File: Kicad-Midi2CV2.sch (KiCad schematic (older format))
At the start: 101 parts, among them IC101 MCP4725module, IC102 MCP4725module, J101 Doepfer connector, J102 Vin 7-12v, J103 MIDI OUT, J104 Power Conn, J105 CV7 in, J106 Gate1, J107 MIDI IN, J108 CV6 in, J109 Gate2, J110 CV3 in, J111 Gate3, J112 CV1, J113 Gate4, J114 CV2, J115 ControlConn, J116 ControlConn, J117 I2C_Conn, J118 I2C_Conn, Q101 MMBT2222A, Q102 MMBT2222A, SW101 KY40_Rotary_Encoder_Module, U101 TL072, U102 TL072, U103 EL814

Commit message: Kicad faliure - unknown state
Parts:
- added D?: LEDset1, LED_THT:LED_D3.0mm_Horizontal_O6.35mm_Z6.0mm, symbol Device:LED
- added R?: 680R, Resistor_SMD:R_0805_2012Metric_Pad1.15x1.40mm_HandSolder, symbol Device:R
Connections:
- wire segments 420 -> 424
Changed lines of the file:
@@
 Text Notes 650  3200 0    79   ~ 16
 MIDI IN
-Text Notes 2875 6125 0    79   ~ 16
+Text Notes 2900 6675 0    79   ~ 16
 LED Signals
 Text Notes 800  6900 0    79   ~ 16
@@
 	750  6300 750  6600
 Wire Wire Line
-	750  5975 750  6300
+	750  5975 750  6100
 Wire Wire Line
 	750  6600 750  7400
@@
 	6550 1350 6550 1175
 Connection ~ 6550 1350
+Text GLabel 3250 6100 2    50   Input ~ 0
+LED_LFO
+$Comp
+L Device:LED D?
+U 1 1 5C593F89
+P 2525 6100
+F 0 "D?" H 2516 6316 50  0000 C CNN
+F 1 "LEDset1" H 2516 6225 50  0000 C CNN
+F 2 "LED_THT:LED_D3.0mm_Horizontal_O6.35mm_Z6.0mm" H 2525 6100 50  0001 C CNN
+F 3 "~" H 2525 6100 50  0001 C CNN
+	1    2525 6100
+	1    0    0    -1
+$EndComp
+$Comp
+L Device:R R?
+U 1 1 5C593F8F
+P 2975 6100
+F 0 "R?" V 2768 6100 50  0000 C CNN
+F 1 "680R" V 2859 6100 50  0000 C CNN
+F 2 "Resistor_SMD:R_0805_2012Metric_Pad1.15x1.40mm_HandSolder" V 2905 6100 50  0001 C CNN
+F 3 "~" H 2975 6100 50  0001 C CNN
+	1    2975 6100
+	0    1    1    0
+$EndComp
+Wire Wire Line
+	2825 6100 2675 6100
+Wire Wire Line
+	3125 6100 3250 6100
+Wire Wire Line
+	2375 6100 750  6100
+Connection ~ 750  6100
+Wire Wire Line
+	750  6100 750  6300
 $EndSCHEMATC

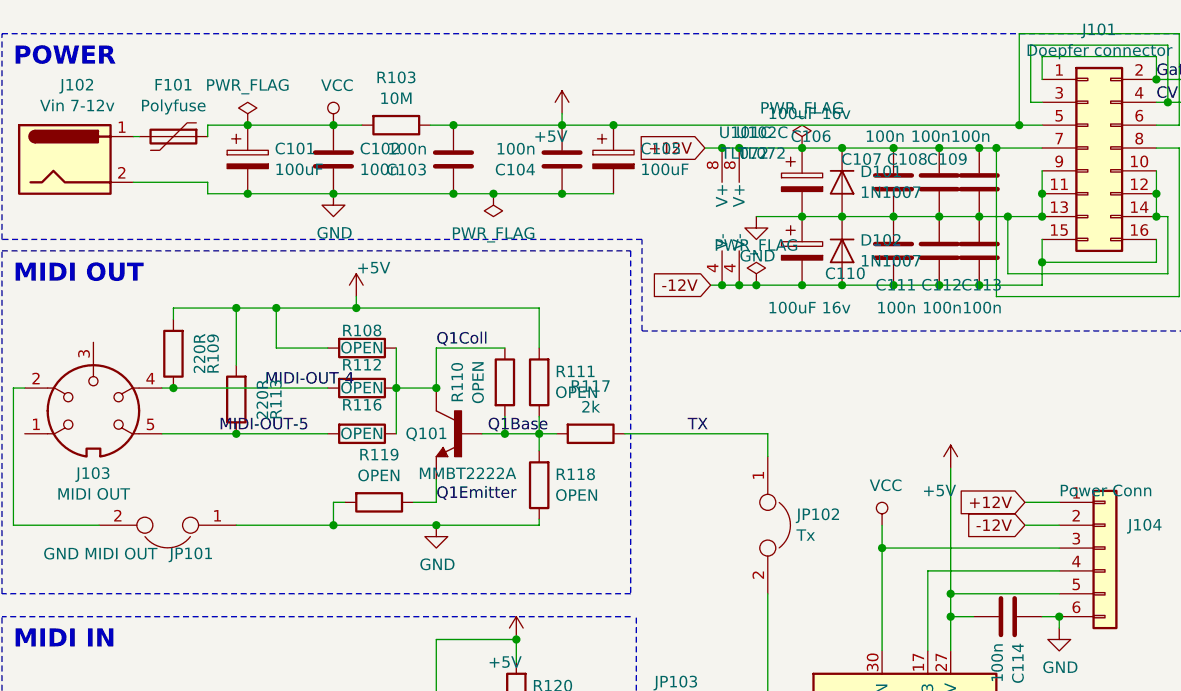
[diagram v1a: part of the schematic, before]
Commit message: Footprints and MIDI out
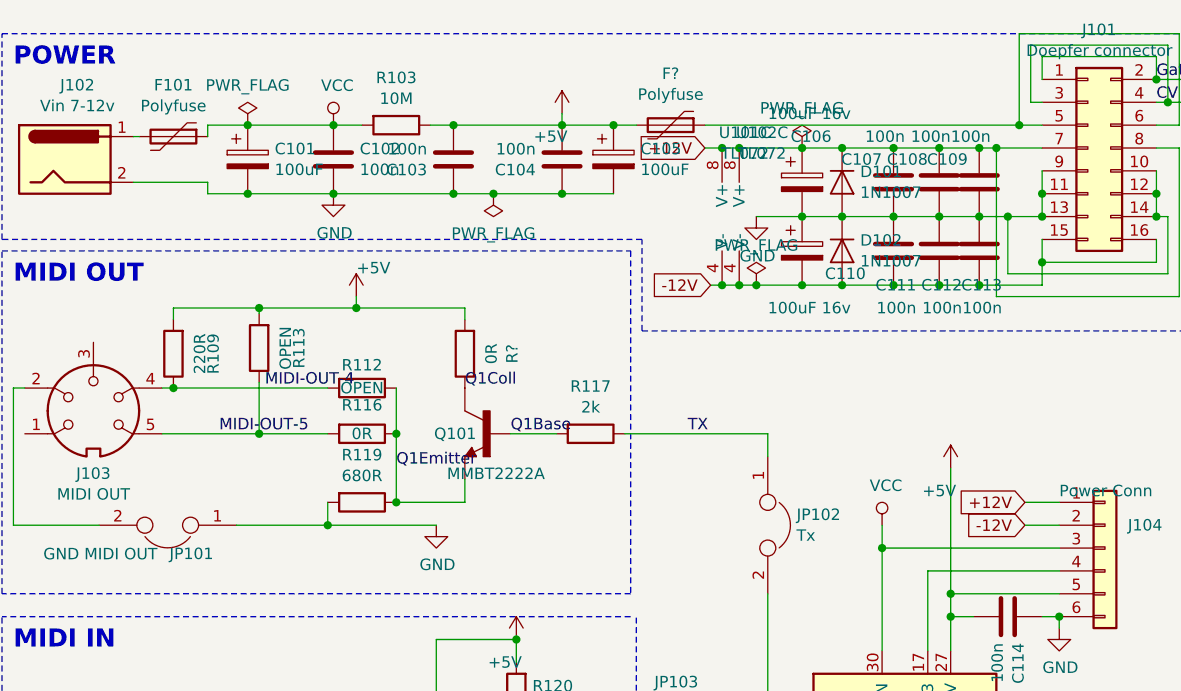
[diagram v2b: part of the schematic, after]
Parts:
- removed R108, R110, R111, R118: OPEN, Resistor_SMD:R_0805_2012Metric_Pad1.15x1.40mm_HandSolder, symbol Device:R
- added F?: Polyfuse, symbol Device:Polyfuse
- added R?: 0R, Resistor_SMD:R_0805_2012Metric_Pad1.15x1.40mm_HandSolder, symbol Device:R
- J104: footprint Connector_PinHeader_2.54mm:PinHeader_1x04_P2.54mm_Vertical -> Connector_PinHeader_2.54mm:PinHeader_1x06_P2.54mm_Vertical
- J115: footprint Connector_PinSocket_2.54mm:PinSocket_1x06_P2.54mm_Vertical -> Connector_PinHeader_2.54mm:PinHeader_1x12_P2.54mm_Vertical
- J116: footprint Connector_PinSocket_2.54mm:PinSocket_1x06_P2.54mm_Vertical -> Connector_PinHeader_2.54mm:PinHeader_1x12_P2.54mm_Horizontal
- J117: footprint Connector_PinSocket_2.54mm:PinSocket_1x06_P2.54mm_Vertical -> Connector_PinHeader_2.54mm:PinHeader_1x08_P2.54mm_Vertical
- J118: footprint Connector_PinSocket_2.54mm:PinSocket_1x06_P2.54mm_Vertical -> Connector_PinHeader_2.54mm:PinHeader_1x08_P2.54mm_Horizontal
- R113: value 220R -> OPEN
- R116: value OPEN -> 0R
- R119: value OPEN -> 680R
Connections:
- wire segments 424 -> 412
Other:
- moved on the sheet: Q101, R113, R119
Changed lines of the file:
@@
 F 0 "J104" H 5525 2850 50  0000 L CNN
 F 1 "Power Conn" H 5225 3000 50  0000 L CNN
-F 2 "Connector_PinHeader_2.54mm:PinHeader_1x04_P2.54mm_Vertical" H 5425 2750 50  0001 C CNN
+F 2 "Connector_PinHeader_2.54mm:PinHeader_1x06_P2.54mm_Vertical" H 5425 2750 50  0001 C CNN
 F 3 "~" H 5425 2750 50  0001 C CNN
 	1    5425 2750
@@
 L MMBT2222A:MMBT2222A Q101
 U 1 1 5C800CB0
-P 2600 2250
-F 0 "Q101" H 2650 2250 50  0000 L CNN
-F 1 "MMBT2222A" H 2350 2075 50  0000 L CNN
-F 2 "Package_TO_SOT_SMD:SOT-23_Handsoldering" H 2600 2250 50  0001 L BNN
-F 3 "Unavailable" H 2600 2250 50  0001 L BNN
-F 4 "None" H 2600 2250 50  0001 L BNN "Field4"
-F 5 "ON" H 2600 2250 50  0001 L BNN "Field5"
-F 6 "MMBT2222A" H 2600 2250 50  0001 L BNN "Field7"
-F 7 "TO-236-3 Taitron" H 2600 2250 50  0001 L BNN "Field8"
-	1    2600 2250
+P 2725 2250
+F 0 "Q101" H 2775 2250 50  0000 L CNN
+F 1 "MMBT2222A" H 2475 2075 50  0000 L CNN
+F 2 "Package_TO_SOT_SMD:SOT-23_Handsoldering" H 2725 2250 50  0001 L BNN
+F 3 "Unavailable" H 2725 2250 50  0001 L BNN
+F 4 "None" H 2725 2250 50  0001 L BNN "Field4"
+F 5 "ON" H 2725 2250 50  0001 L BNN "Field5"
+F 6 "MMBT2222A" H 2725 2250 50  0001 L BNN "Field7"
+F 7 "TO-236-3 Taitron" H 2725 2250 50  0001 L BNN "Field8"
+	1    2725 2250
 	-1   0    0    -1
-$EndComp
-$Comp
-L Device:R R111
-U 1 1 5C800E88
-P 2950 2025
-F 0 "R111" H 2880 1979 50  0000 R CNN
-F 1 "OPEN" H 2880 2070 50  0000 R CNN
-F 2 "Resistor_SMD:R_0805_2012Metric_Pad1.15x1.40mm_HandSolder" V 2880 2025 50  0001 C CNN
-F 3 "~" H 2950 2025 50  0001 C CNN
-	1    2950 2025
-	-1   0    0    1
-$EndComp
-$Comp
-L Device:R R118
-U 1 1 5C800F7E
-P 2950 2475
-F 0 "R118" H 2880 2429 50  0000 R CNN
-F 1 "OPEN" H 2880 2520 50  0000 R CNN
-F 2 "Resistor_SMD:R_0805_2012Metric_Pad1.15x1.40mm_HandSolder" V 2880 2475 50  0001 C CNN
-F 3 "~" H 2950 2475 50  0001 C CNN
-	1    2950 2475
-	-1   0    0    1
 $EndComp
 $Comp
@@
 Wire Wire Line
 	3950 3700 3950 2950
-Connection ~ 2500 2650
 Wire Wire Line
 	2150 1700 2150 1650
@@
 Connection ~ 5050 900
 Wire Wire Line
-	5050 900  3275 900
+	5050 900  3675 900
 Wire Wire Line
 	5650 1500 5650 1400
@@
 F 0 "J117" H 6623 7005 50  0000 R CNN
 F 1 "I2C_Conn" H 6800 7425 50  0000 R CNN
-F 2 "Connector_PinSocket_2.54mm:PinSocket_1x06_P2.54mm_Vertical" H 6650 7125 50  0001 C CNN
+F 2 "Connector_PinHeader_2.54mm:PinHeader_1x08_P2.54mm_Vertical" H 6650 7125 50  0001 C CNN
 F 3 "~" H 6650 7125 50  0001 C CNN
 	1    6650 7125
@@
 F 0 "J118" H 6173 7055 50  0000 R CNN
 F 1 "I2C_Conn" H 6350 7425 50  0000 R CNN
-F 2 "Connector_PinSocket_2.54mm:PinSocket_1x06_P2.54mm_Vertical" H 6200 7175 50  0001 C CNN
+F 2 "Connector_PinHeader_2.54mm:PinHeader_1x08_P2.54mm_Horizontal" H 6200 7175 50  0001 C CNN
 F 3 "~" H 6200 7175 50  0001 C CNN
 	1    6200 7175
@@
 F 0 "J116" H 4523 6805 50  0000 R CNN
 F 1 "ControlConn" H 4650 7500 50  0000 R CNN
-F 2 "Connector_PinSocket_2.54mm:PinSocket_1x06_P2.54mm_Vertical" H 4550 6925 50  0001 C CNN
+F 2 "Connector_PinHeader_2.54mm:PinHeader_1x12_P2.54mm_Horizontal" H 4550 6925 50  0001 C CNN
 F 3 "~" H 4550 6925 50  0001 C CNN
 	1    4550 6925
@@
 L Device:R R113
 U 1 1 5C5491E2
-P 1625 2100
-F 0 "R113" V 1450 2100 50  0000 C CNN
-F 1 "220R" V 1509 2100 50  0000 C CNN
-F 2 "Resistor_SMD:R_0805_2012Metric_Pad1.15x1.40mm_HandSolder" V 1555 2100 50  0001 C CNN
-F 3 "~" H 1625 2100 50  0001 C CNN
-	1    1625 2100
+P 1725 1875
+F 0 "R113" V 1550 1875 50  0000 C CNN
+F 1 "OPEN" V 1609 1875 50  0000 C CNN
+F 2 "Resistor_SMD:R_0805_2012Metric_Pad1.15x1.40mm_HandSolder" V 1655 1875 50  0001 C CNN
+F 3 "~" H 1725 1875 50  0001 C CNN
+	1    1725 1875
 	-1   0    0    1
 $EndComp
-Wire Wire Line
-	1800 1700 2150 1700
 $Comp
 L Device:R R117
@@
 $EndComp
 $Comp
-L Device:R R110
-U 1 1 5C589676
-P 2800 2025
-F 0 "R110" V 2593 2025 50  0000 C CNN
-F 1 "OPEN" V 2684 2025 50  0000 C CNN
-F 2 "Resistor_SMD:R_0805_2012Metric_Pad1.15x1.40mm_HandSolder" V 2730 2025 50  0001 C CNN
-F 3 "~" H 2800 2025 50  0001 C CNN
-	1    2800 2025
-	1    0    0    -1
-$EndComp
-$Comp
 L Device:R R119
 U 1 1 5C5CBC55
-P 2250 2550
-F 0 "R119" V 2043 2550 50  0000 C CNN
-F 1 "OPEN" V 2134 2550 50  0000 C CNN
-F 2 "Resistor_SMD:R_0805_2012Metric_Pad1.15x1.40mm_HandSolder" V 2180 2550 50  0001 C CNN
-F 3 "~" H 2250 2550 50  0001 C CNN
-	1    2250 2550
+P 2175 2550
+F 0 "R119" V 1968 2550 50  0000 C CNN
+F 1 "680R" V 2059 2550 50  0000 C CNN
+F 2 "Resistor_SMD:R_0805_2012Metric_Pad1.15x1.40mm_HandSolder" V 2105 2550 50  0001 C CNN
+F 3 "~" H 2175 2550 50  0001 C CNN
+	1    2175 2550
 	0    1    1    0
 $EndComp
@@
 Wire Wire Line
 	650  2650 1025 2650
-Wire Wire Line
-	3025 2250 2950 2250
-Wire Wire Line
-	2800 2175 2800 2250
-Connection ~ 2800 2250
-Wire Wire Line
-	2800 2250 2700 2250
-Wire Wire Line
-	2950 2625 2950 2650
-Wire Wire Line
-	2950 2650 2500 2650
-Wire Wire Line
-	2100 2550 2050 2550
-Wire Wire Line
-	2050 2550 2050 2650
-Connection ~ 2050 2650
-Wire Wire Line
-	2050 2650 2500 2650
-Wire Wire Line
-	2400 2550 2500 2550
-Wire Wire Line
-	2500 2550 2500 2450
-Wire Wire Line
-	2950 1875 2950 1700
-Wire Wire Line
-	2950 1700 2150 1700
-Connection ~ 2150 1700
-Wire Wire Line
-	2800 1875 2500 1875
-Wire Wire Line
-	2500 1875 2500 2050
 $Comp
 L Device:R R112
@@
 $EndComp
 $Comp
-L Device:R R108
-U 1 1 5C78F59B
-P 2175 1875
-F 0 "R108" V 2100 1875 50  0000 C CNN
-F 1 "OPEN" V 2175 1875 50  0000 C CNN
-F 2 "Resistor_SMD:R_0805_2012Metric_Pad1.15x1.40mm_HandSolder" V 2105 1875 50  0001 C CNN
-F 3 "~" H 2175 1875 50  0001 C CNN
-	1    2175 1875
-	0    1    1    0
-$EndComp
-Connection ~ 2500 2050
-$Comp
 L Device:R R116
 U 1 1 5C7FDED9
 P 2175 2250
 F 0 "R116" V 2050 2250 50  0000 C CNN
-F 1 "OPEN" V 2175 2250 50  0000 C CNN
+F 1 "0R" V 2175 2250 50  0000 C CNN
 F 2 "Resistor_SMD:R_0805_2012Metric_Pad1.15x1.40mm_HandSolder" V 2105 2250 50  0001 C CNN
 F 3 "~" H 2175 2250 50  0001 C CNN
@@
 Wire Wire Line
 	2325 2250 2325 2050
-Connection ~ 2325 2050
-Wire Wire Line
-	2325 2050 2500 2050
-Wire Wire Line
-	2325 1875 2325 2050
-Wire Wire Line
-	2025 1875 1800 1875
-Wire Wire Line
-	1800 1875 1800 1700
-Wire Wire Line
-	1300 2250 1625 2250
 Wire Wire Line
 	1350 2050 2025 2050
 Connection ~ 1350 2050
-Connection ~ 1625 2250
-Wire Wire Line
-	1625 2250 2025 2250
-Wire Wire Line
-	1625 1950 1625 1700
-Connection ~ 1800 1700
 Wire Wire Line
 	1350 1750 1350 1700
-Wire Wire Line
-	1350 1700 1625 1700
-Connection ~ 1625 1700
-Wire Wire Line
-	1625 1700 1800 1700
-Wire Wire Line
-	2950 2175 2950 2250
-Connection ~ 2950 2250
-Wire Wire Line
-	2950 2250 2800 2250
-Wire Wire Line
-	2950 2250 2950 2325
 $Comp
 L Device:Jumper JP101
@@
 	-1   0    0    1
 $EndComp
-Wire Wire Line
-	1625 2650 2050 2650
 Text Label 1550 2250 0    50   ~ 0
 MIDI-OUT-5
-Text Label 2500 1875 0    50   ~ 0
+Text Label 2625 2050 0    50   ~ 0
 Q1Coll
-Text Label 2725 2250 0    50   ~ 0
+Text Label 2825 2250 0    50   ~ 0
 Q1Base
-Text Label 2500 2550 0    50   ~ 0
+Text Label 2325 2400 0    50   ~ 0
 Q1Emitter
 Text Label 2975 3600 0    50   ~ 0
@@
 F 0 "J115" H 4873 6730 50  0000 R CNN
 F 1 "ControlConn" H 5000 7425 50  0000 R CNN
-F 2 "Connector_PinSocket_2.54mm:PinSocket_1x06_P2.54mm_Vertical" H 4900 6850 50  0001 C CNN
+F 2 "Connector_PinHeader_2.54mm:PinHeader_1x12_P2.54mm_Vertical" H 4900 6850 50  0001 C CNN
 F 3 "~" H 4900 6850 50  0001 C CNN
 	1    4900 6850
@@
 Wire Wire Line
 	750  6100 750  6300
+Wire Wire Line
+	1625 2650 2025 2650
+Connection ~ 2025 2650
+Wire Wire Line
+	2025 2650 2500 2650
+Wire Wire Line
+	2025 2550 2025 2650
+Wire Wire Line
+	2325 2550 2625 2550
+Wire Wire Line
+	2625 2550 2625 2450
+Wire Wire Line
+	2825 2250 3025 2250
+Wire Wire Line
+	2150 1700 2625 1700
+Connection ~ 2150 1700
+Wire Wire Line
+	2325 2250 2325 2550
+Connection ~ 2325 2250
+Connection ~ 2325 2550
+Wire Wire Line
+	1725 1725 1725 1700
+Wire Wire Line
+	1300 2250 1725 2250
+Connection ~ 1725 1700
+Wire Wire Line
+	1725 1700 2150 1700
+Wire Wire Line
+	1725 2025 1725 2250
+Connection ~ 1725 2250
+Wire Wire Line
+	1725 2250 2025 2250
+Wire Wire Line
+	1350 1700 1725 1700
+Wire Wire Line
+	2625 1700 2625 1750
+$Comp
+L Device:R R?
+U 1 1 5C668F91
+P 2625 1900
+F 0 "R?" V 2418 1900 50  0000 C CNN
+F 1 "0R" V 2509 1900 50  0000 C CNN
+F 2 "Resistor_SMD:R_0805_2012Metric_Pad1.15x1.40mm_HandSolder" V 2555 1900 50  0001 C CNN
+F 3 "~" H 2625 1900 50  0001 C CNN
+	1    2625 1900
+	-1   0    0    1
+$EndComp
+$Comp
+L Device:Polyfuse F?
+U 1 1 5C8D3169
+P 3525 900
+F 0 "F?" V 3300 900 50  0000 C CNN
+F 1 "Polyfuse" V 3391 900 50  0000 C CNN
+F 2 "" H 3575 700 50  0001 L CNN
+F 3 "~" H 3525 900 50  0001 C CNN
+	1    3525 900
+	0    1    1    0
+$EndComp
+Wire Wire Line
+	3375 900  3275 900
 $EndSCHEMATC

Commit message: MIDI out simplified #1
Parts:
- gave numbers to parts that had none: 4
- renumbered D109 to D110, D110 to D111, F101 to F102, R113 to R108, R112 to R111, R114 to R112, R115 to R113, R116 to R114, R117 to R115, R119 to R116, R120 to R117, R121 to R118, R122 to R119, R123 to R120, R124 to R121, R125 to R122, R126 to R123, R127 to R124, R128 to R125, R129 to R126, R130 to R127, R131 to R128, R132 to R129, R133 to R130, R134 to R131, R135 to R132, R136 to R133, R137 to R134, R138 to R136, R139 to R137, R140 to R138

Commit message: Footprint replace in sch, netlist and PCB
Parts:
- J106, J109, J112, J114: footprint Connector_Audio:AudioJack3StereoNarrow-PJ-321 -> AJ-Dropbox-Kicad:PJ301SM
- R110, R114: footprint Resistor_SMD:R_0805_2012Metric_Pad1.15x1.40mm_HandSolder -> Jumper:SolderJumper-2_P1.3mm_Bridged_RoundedPad1.0x1.5mm
- RV101, RV102: footprint Potentiometer_THT:Potentiometer_Alps_RK097_Single_Horizontal -> Potentiometer_THT:Potentiometer_Alps_RK09K_Single_Vertical
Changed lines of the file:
@@
 F 0 "J112" H 6667 4971 50  0000 R CNN
 F 1 "CV1" H 6667 4880 50  0000 R CNN
-F 2 "Connector_Audio:AudioJack3StereoNarrow-PJ-321" H 6900 4900 50  0001 C CNN
+F 2 "AJ-Dropbox-Kicad:PJ301SM" H 6900 4900 50  0001 C CNN
 F 3 "~" H 6900 4900 50  0001 C CNN
 F 4 "CV1 Out" H 6900 4900 50  0001 C CNN "Function"
@@
 F 0 "J114" H 6667 5271 50  0000 R CNN
 F 1 "CV2" H 6667 5180 50  0000 R CNN
-F 2 "Connector_Audio:AudioJack3StereoNarrow-PJ-321" H 6900 5200 50  0001 C CNN
+F 2 "AJ-Dropbox-Kicad:PJ301SM" H 6900 5200 50  0001 C CNN
 F 3 "~" H 6900 5200 50  0001 C CNN
 F 4 "CV2 out" H 6900 5200 50  0001 C CNN "Function"
@@
 F 0 "J106" H 7967 3671 50  0000 R CNN
 F 1 "Gate1" H 7967 3580 50  0000 R CNN
-F 2 "Connector_Audio:AudioJack3StereoNarrow-PJ-321" H 8200 3600 50  0001 C CNN
+F 2 "AJ-Dropbox-Kicad:PJ301SM" H 8200 3600 50  0001 C CNN
 F 3 "~" H 8200 3600 50  0001 C CNN
 	1    8200 3600
@@
 F 0 "J109" H 7967 4121 50  0000 R CNN
 F 1 "Gate2" H 7967 4030 50  0000 R CNN
-F 2 "Connector_Audio:AudioJack3StereoNarrow-PJ-321" H 8200 4050 50  0001 C CNN
+F 2 "AJ-Dropbox-Kicad:PJ301SM" H 8200 4050 50  0001 C CNN
 F 3 "~" H 8200 4050 50  0001 C CNN
 	1    8200 4050
@@
 F 0 "RV102" H 10355 2421 50  0000 R CNN
 F 1 "10k" H 10355 2330 50  0000 R CNN
-F 2 "Potentiometer_THT:Potentiometer_Alps_RK097_Single_Horizontal" H 10425 2375 50  0001 C CNN
+F 2 "Potentiometer_THT:Potentiometer_Alps_RK09K_Single_Vertical" H 10425 2375 50  0001 C CNN
 F 3 "~" H 10425 2375 50  0001 C CNN
 	1    10425 2375
@@
 F 0 "RV101" H 10305 1246 50  0000 R CNN
 F 1 "10k" H 10305 1155 50  0000 R CNN
-F 2 "Potentiometer_THT:Potentiometer_Alps_RK097_Single_Horizontal" H 10375 1200 50  0001 C CNN
+F 2 "Potentiometer_THT:Potentiometer_Alps_RK09K_Single_Vertical" H 10375 1200 50  0001 C CNN
 F 3 "~" H 10375 1200 50  0001 C CNN
 	1    10375 1200
@@
 F 0 "R114" V 2050 2250 50  0000 C CNN
 F 1 "0R" V 2175 2250 50  0000 C CNN
-F 2 "Resistor_SMD:R_0805_2012Metric_Pad1.15x1.40mm_HandSolder" V 2105 2250 50  0001 C CNN
+F 2 "Jumper:SolderJumper-2_P1.3mm_Bridged_RoundedPad1.0x1.5mm" V 2105 2250 50  0001 C CNN
 F 3 "~" H 2175 2250 50  0001 C CNN
 	1    2175 2250
@@
 F 0 "R110" V 2418 1900 50  0000 C CNN
 F 1 "0R" V 2509 1900 50  0000 C CNN
-F 2 "Resistor_SMD:R_0805_2012Metric_Pad1.15x1.40mm_HandSolder" V 2555 1900 50  0001 C CNN
+F 2 "Jumper:SolderJumper-2_P1.3mm_Bridged_RoundedPad1.0x1.5mm" V 2555 1900 50  0001 C CNN
 F 3 "~" H 2625 1900 50  0001 C CNN
 	1    2625 1900

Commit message: Footprints and LED labels
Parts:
- D104, D105, D106, D107: footprint LED_THT:LED_D3.0mm_Horizontal_O6.35mm_Z6.0mm -> LED_THT:LED_D3.0mm
- D108: value LEDset1 -> LED_MIDI; footprint LED_THT:LED_D3.0mm_Horizontal_O6.35mm_Z6.0mm -> LED_THT:LED_D3.0mm
- D109: value LEDset1 -> LED_LFO; footprint LED_THT:LED_D3.0mm_Horizontal_O6.35mm_Z6.0mm -> LED_THT:LED_D3.0mm
- D110: value LEDset2 -> LED_CV1; footprint LED_THT:LED_D3.0mm_Horizontal_O6.35mm_Z6.0mm -> LED_THT:LED_D3.0mm
- D111: value LEDset2 -> LED_CV2; footprint LED_THT:LED_D3.0mm_Horizontal_O6.35mm_Z6.0mm -> LED_THT:LED_D3.0mm
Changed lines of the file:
@@
 F 0 "D104" H 1091 5016 50  0000 C CNN
 F 1 "LED1" H 1091 4925 50  0000 C CNN
-F 2 "LED_THT:LED_D3.0mm_Horizontal_O6.35mm_Z6.0mm" H 1100 4800 50  0001 C CNN
+F 2 "LED_THT:LED_D3.0mm" H 1100 4800 50  0001 C CNN
 F 3 "~" H 1100 4800 50  0001 C CNN
 	1    1100 4800
@@
 F 0 "D105" H 1091 5316 50  0000 C CNN
 F 1 "LED2" H 1091 5225 50  0000 C CNN
-F 2 "LED_THT:LED_D3.0mm_Horizontal_O6.35mm_Z6.0mm" H 1100 5100 50  0001 C CNN
+F 2 "LED_THT:LED_D3.0mm" H 1100 5100 50  0001 C CNN
 F 3 "~" H 1100 5100 50  0001 C CNN
 	1    1100 5100
@@
 F 0 "D106" H 1091 5616 50  0000 C CNN
 F 1 "LED3" H 1091 5525 50  0000 C CNN
-F 2 "LED_THT:LED_D3.0mm_Horizontal_O6.35mm_Z6.0mm" H 1100 5400 50  0001 C CNN
+F 2 "LED_THT:LED_D3.0mm" H 1100 5400 50  0001 C CNN
 F 3 "~" H 1100 5400 50  0001 C CNN
 	1    1100 5400
@@
 F 0 "D107" H 1091 5891 50  0000 C CNN
 F 1 "LED4" H 1091 5800 50  0000 C CNN
-F 2 "LED_THT:LED_D3.0mm_Horizontal_O6.35mm_Z6.0mm" H 1100 5675 50  0001 C CNN
+F 2 "LED_THT:LED_D3.0mm" H 1100 5675 50  0001 C CNN
 F 3 "~" H 1100 5675 50  0001 C CNN
 	1    1100 5675
@@
 P 1100 5975
 F 0 "D108" H 1091 6191 50  0000 C CNN
-F 1 "LEDset1" H 1091 6100 50  0000 C CNN
-F 2 "LED_THT:LED_D3.0mm_Horizontal_O6.35mm_Z6.0mm" H 1100 5975 50  0001 C CNN
+F 1 "LED_MIDI" H 1091 6100 50  0000 C CNN
+F 2 "LED_THT:LED_D3.0mm" H 1100 5975 50  0001 C CNN
 F 3 "~" H 1100 5975 50  0001 C CNN
 	1    1100 5975
@@
 P 1100 6300
 F 0 "D110" H 1091 6516 50  0000 C CNN
-F 1 "LEDset2" H 1091 6425 50  0000 C CNN
-F 2 "LED_THT:LED_D3.0mm_Horizontal_O6.35mm_Z6.0mm" H 1100 6300 50  0001 C CNN
+F 1 "LED_CV1" H 1091 6425 50  0000 C CNN
+F 2 "LED_THT:LED_D3.0mm" H 1100 6300 50  0001 C CNN
 F 3 "~" H 1100 6300 50  0001 C CNN
 	1    1100 6300
@@
 P 1100 6600
 F 0 "D111" H 1091 6816 50  0000 C CNN
-F 1 "LEDset2" H 1091 6725 50  0000 C CNN
-F 2 "LED_THT:LED_D3.0mm_Horizontal_O6.35mm_Z6.0mm" H 1100 6600 50  0001 C CNN
+F 1 "LED_CV2" H 1091 6725 50  0000 C CNN
+F 2 "LED_THT:LED_D3.0mm" H 1100 6600 50  0001 C CNN
 F 3 "~" H 1100 6600 50  0001 C CNN
 	1    1100 6600
@@
 U 1 1 5C593F89
 P 2525 6100
-F 0 "D109" H 2516 6316 50  0000 C CNN
-F 1 "LEDset1" H 2516 6225 50  0000 C CNN
-F 2 "LED_THT:LED_D3.0mm_Horizontal_O6.35mm_Z6.0mm" H 2525 6100 50  0001 C CNN
+F 0 "D109" H 2350 6125 50  0000 C CNN
+F 1 "LED_LFO" H 2750 6025 50  0000 C CNN
+F 2 "LED_THT:LED_D3.0mm" H 2525 6100 50  0001 C CNN
 F 3 "~" H 2525 6100 50  0001 C CNN
 	1    2525 6100

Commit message: Jumper fixes
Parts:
- F101, F102: footprint (none) -> Fuse:Fuse_1206_3216Metric_Pad1.42x1.75mm_HandSolder
- J115: footprint Connector_PinHeader_2.54mm:PinHeader_1x12_P2.54mm_Vertical -> Connector_PinHeader_2.54mm:PinHeader_1x11_P2.54mm_Vertical; symbol Connector:Conn_01x12_Male -> Connector:Conn_01x11_Male
- J116: footprint Connector_PinHeader_2.54mm:PinHeader_1x12_P2.54mm_Horizontal -> Connector_PinHeader_2.54mm:PinHeader_1x11_P2.54mm_Horizontal; symbol Connector:Conn_01x12_Male -> Connector:Conn_01x11_Male
- J117: footprint Connector_PinHeader_2.54mm:PinHeader_1x08_P2.54mm_Vertical -> Connector_PinHeader_2.54mm:PinHeader_1x09_P2.54mm_Vertical; symbol Connector:Conn_01x08_Male -> Connector:Conn_01x09_Male
- J118: footprint Connector_PinHeader_2.54mm:PinHeader_1x08_P2.54mm_Horizontal -> Connector_PinHeader_2.54mm:PinHeader_1x09_P2.54mm_Horizontal; symbol Connector:Conn_01x08_Male -> Connector:Conn_01x09_Male
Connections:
- wire segments 412 -> 410
